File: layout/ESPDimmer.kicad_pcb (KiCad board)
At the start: 2 copper layers, 36 x 31 mm, 13 parts, among them P1 CONN_01X03, P2 Serial, P3 LED, P4 ProgMod, P5 DS18B20, Q1 IRLB8721, U1 TLV1117-33, U2 ESP-12E

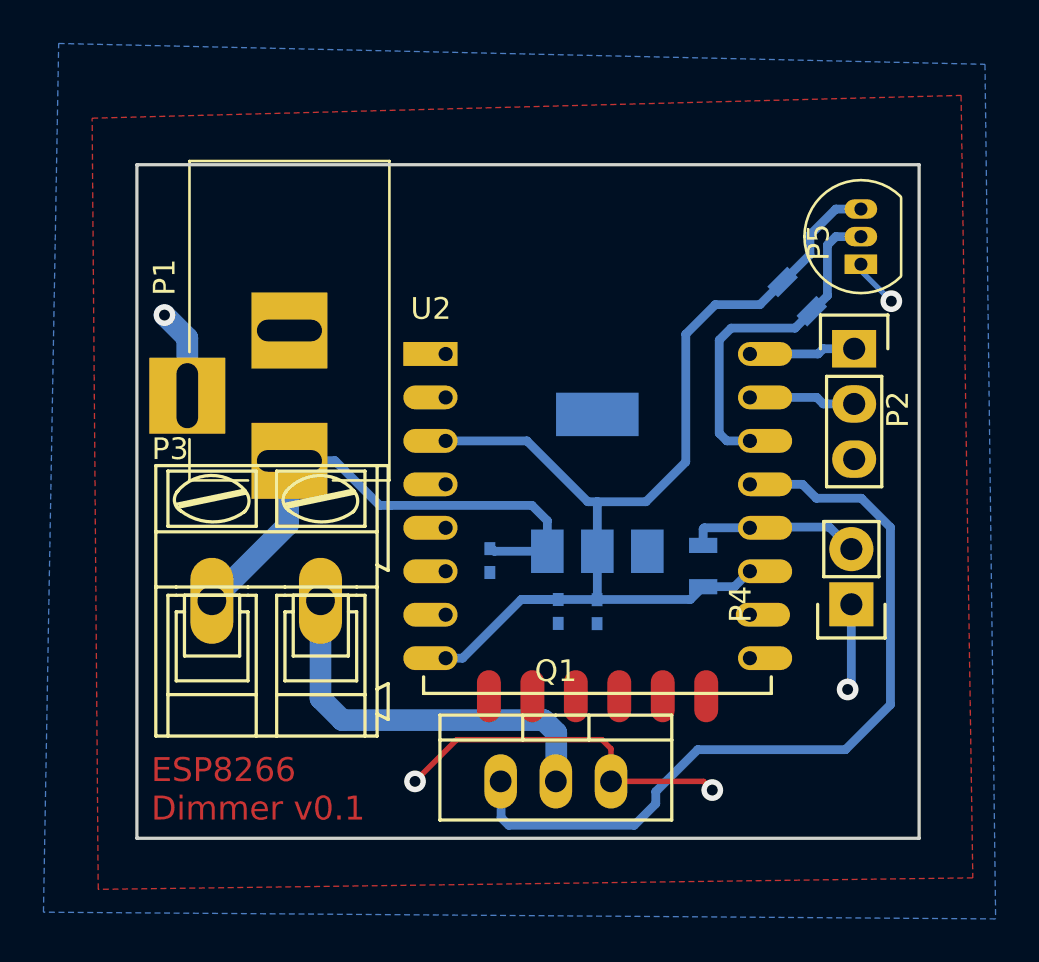
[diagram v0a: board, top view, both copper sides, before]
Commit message: Removed thermometer because its readings were incorrect due to the thermal release of the voltage regulator
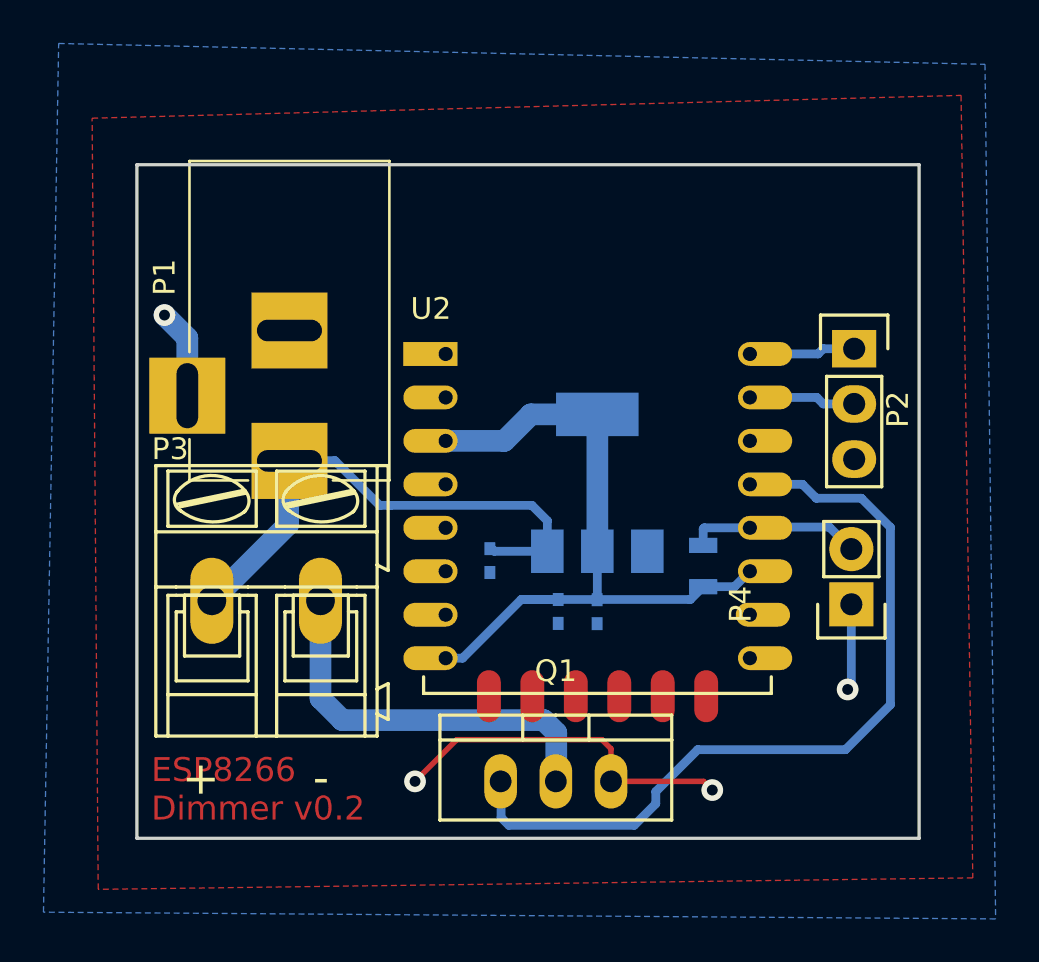
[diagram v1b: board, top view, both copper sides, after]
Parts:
- removed P5: DS18B20, TO_SOT_Packages_THT:TO-92_Inline_Narrow_Oval
- removed R2: 4k7, Resistors_SMD:R_0805
- U1: value TLV1117-33 -> TLV1117
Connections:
- U1 pad 4: (no net) -> +3V3
- U2 pad 1: (no net) -> Net-(U2-Pad1)
- U2 pad 17: (no net) -> Net-(U2-Pad17)
- U2 pad 18: (no net) -> Net-(U2-Pad18)
- U2 pad 19: (no net) -> Net-(U2-Pad19)
- U2 pad 2: (no net) -> Net-(U2-Pad2)
- U2 pad 20: (no net) -> Net-(U2-Pad20)
- U2 pad 21: (no net) -> Net-(U2-Pad21)
- U2 pad 22: (no net) -> Net-(U2-Pad22)
- U2 pad 4: (no net) -> Net-(U2-Pad4)
- U2 pad 5: (no net) -> Net-(U2-Pad5)
- U2 pad 6: (no net) -> Net-(U2-Pad6)
- U2 pad 7: (no net) -> Net-(U2-Pad7)
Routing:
- net +3V3: track 51.7 -> 33.4 mm
- net Net-(U2-Pad14): track 15.7 -> 0.00 mm
- net GND: track 26.7 -> 24.5 mm, vias 5 -> 4
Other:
- board text added: "+"
- board text added: "-"
- board text added: "ESP8266 Dimmer v0.2"
- board text removed: "ESP8266 Dimmer v0.1"
